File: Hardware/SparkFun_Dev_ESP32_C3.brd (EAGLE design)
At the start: 17.8 x 33 mm, 37 parts, among them J1 USB Female Type C Connector, J4 QWIIC_RIGHT_ANGLE, U1 ESP32-C3, U2 RT9080-33GJ5, Y1 40MHZ

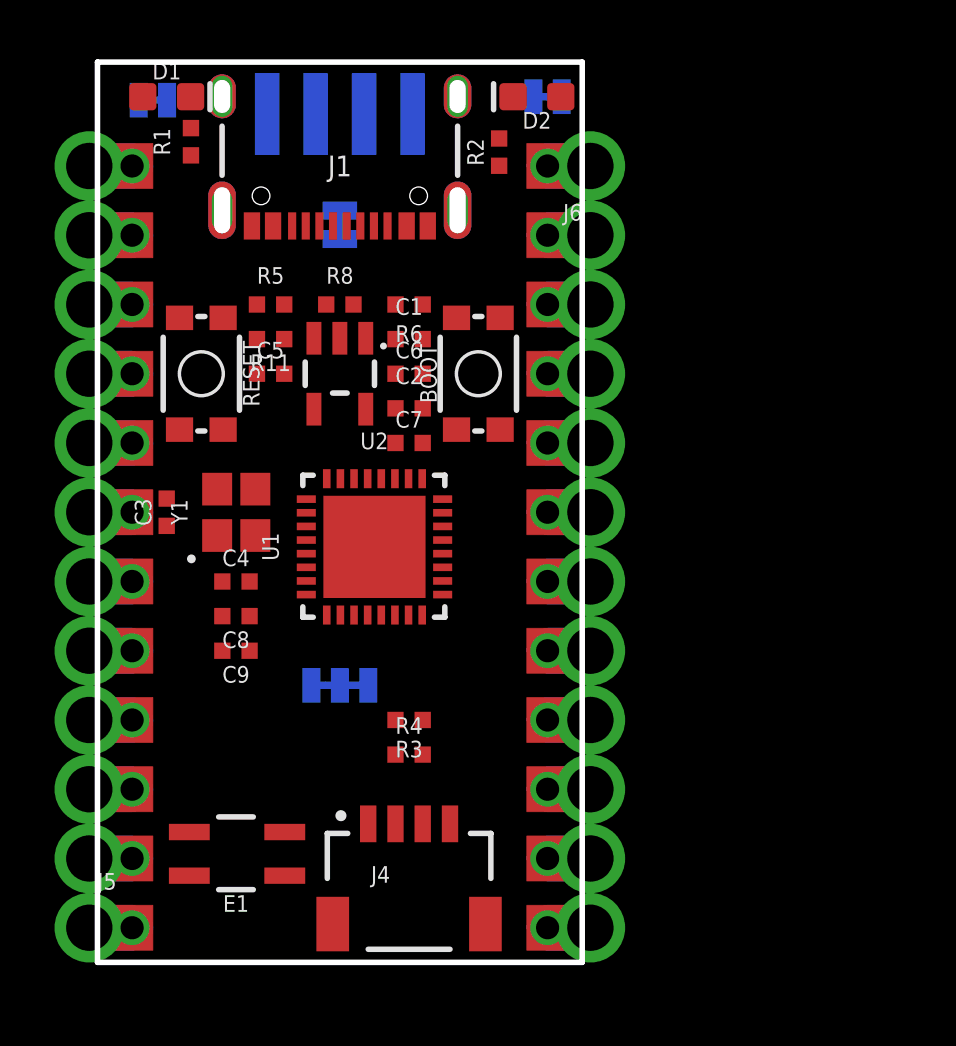
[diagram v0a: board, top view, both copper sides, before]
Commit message: Adds JTAG header and corrects boot control configuration
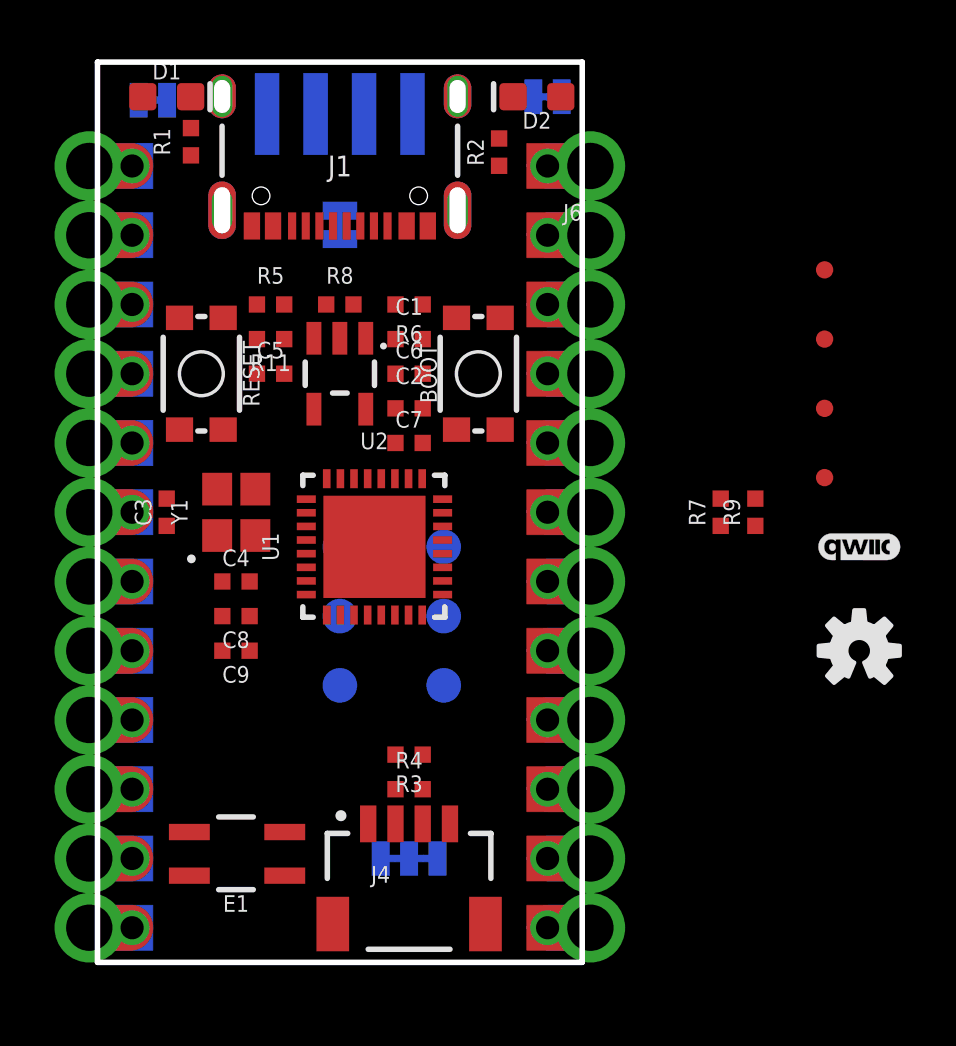
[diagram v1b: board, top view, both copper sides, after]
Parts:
- added FD1, FD2, FD3, FD4: FIDUCIALUFIDUCIAL, SparkFun-Aesthetics:FIDUCIAL-MICRO
- added LOGO2: QWIIC_LOGO_3MM, SparkFun-Aesthetics:QWIIC_3MM
- added LOGO3: OSHW-LOGOS, SparkFun-Aesthetics:OSHW-LOGO-S
- added R7, R9: 100k, SparkFun-Resistors:0402-TIGHT
- added TP1, TP2, TP3, TP4, TP5, TP6: TEST-POINT3X5, SparkFun-Connectors:PAD.03X.05
- moved J5 27.9 mm to (2.54, 29.2), flipped to the bottom, turned to 180 degrees
- moved I2C 6.84 mm to (12.7, 3.81)
- moved R3 1.27 mm to (12.7, 7.62)
- moved R4 1.27 mm to (12.7, 6.35)
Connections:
- removed net IO20/TX: J5.12, J5.12B, U1.P27
- removed net IO21/RX: J5.11, J5.11B, U1.P28
- removed net IO4/A4: U1.P9
- removed net IO5/A5: J6.6, J6.6B, U1.P10
- removed net IO6/SCLK: J6.9, J6.9B, U1.P12
- removed net IO7/PICO: J6.11, J6.11B, U1.P13
- removed net IO8/BOOT: BOOT.3, BOOT.4, C6.1, U1.P14
- new net IO20/TXO: U1.P27
- new net IO21/RXI: U1.P28
- new net IO4/A4/MTMS: J6.5, J6.5B, TP4.1, U1.P9
- new net IO5/A5/MTDI: TP6.1, U1.P10
- new net IO6/SCLK/MTCK: J6.9, J6.9B, TP3.1, U1.P12
- new net IO7/PICO/MTDO: J6.11, J6.11B, TP1.1, U1.P13
- new net IO8: R7.1, U1.P14
- new net IO9/BOOT: BOOT.3, BOOT.4, C6.1, U1.P15
- new net NC: J5.10, J5.10B, J5.9, J5.9B
- net 3.3V: now also R7.2, R9.2
- net EN: now also TP5.1
- net GND: now also J5.3, J5.3B, J5.4, J5.4B, TP2.1; no longer J5.10, J5.10B, J5.9, J5.9B
- net IO10: no longer J5.8, J5.8B
- net IO12: no longer J5.7, J5.7B
- net IO13/SDA: no longer J5.2, J5.2B
- net IO14/SCL: no longer J5.1, J5.1B
- net IO15: no longer J5.6, J5.6B
- net IO16: no longer J5.5, J5.5B
- net IO2/POCI: now also R9.1
- net IO3/A3: now also J6.6, J6.6B; no longer J6.5, J6.5B

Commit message: Moves any connections away from antenna
* Finishes netting
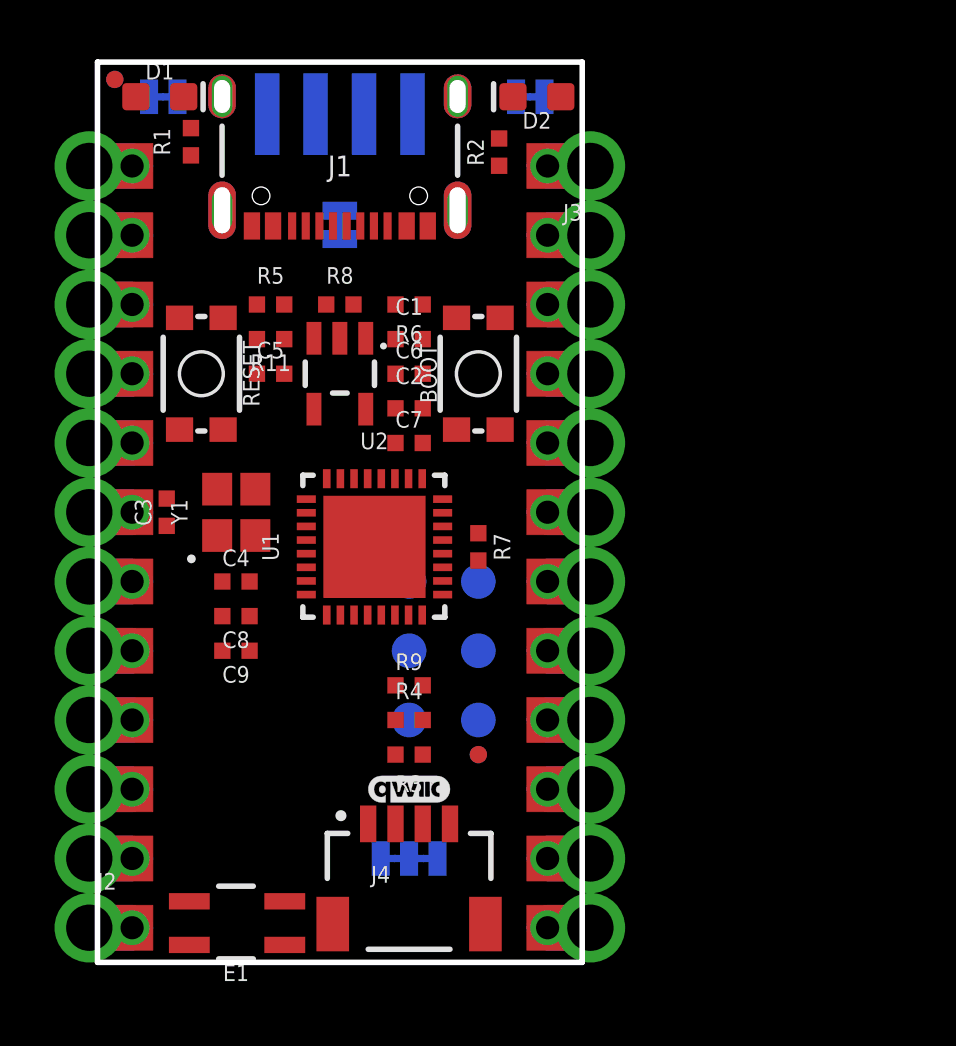
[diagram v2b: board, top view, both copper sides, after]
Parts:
- removed J5, J6: (no value), Castellated:1X12_CASTELLATED
- added J2, J3: (no value), SparkFun-Connectors:1X12_CASTELLATED
- moved FD2 27.7 mm to (1.91, 32.4), flipped to the bottom
- moved FD1 27.0 mm to (1.91, 32.4)
- moved LOGO3 23.0 mm to (6.35, 8.89), flipped to the bottom
- moved LOGO2 18.8 mm to (12.7, 6.35)
- moved FD3 18.0 mm to (15.2, 7.62)
- moved FD4 16.3 mm to (15.2, 7.62), flipped to the bottom
- moved R9 14.2 mm to (12.7, 10.2), turned to 0 degrees
- moved R7 8.98 mm to (15.2, 15.2), turned to 270 degrees
- moved TP4 2.84 mm to (12.7, 8.89)
- moved TP5 2.84 mm to (12.7, 11.4)
- moved TP6 2.84 mm to (12.7, 14.0)
- moved R4 2.54 mm to (12.7, 8.89)
- moved E1 2.54 mm to (6.35, 1.27)
- moved TP1 1.80 mm to (15.2, 14.0)
- moved TP2 1.80 mm to (15.2, 11.4)
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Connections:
- removed net !RESET!: J6.3, J6.3B
- removed net IO6/SDA: J4.3
- removed net IO7/SCL: J4.4
- removed net RAW: J6.1, J6.1B
- net 3.3V: now also J3.4, J3.4B; no longer J6.4, J6.4B
- net EN: now also J3.3, J3.3B
- net GND: now also J2.10, J2.10B, J2.9, J2.9B, J3.2, J3.2B; no longer J5.3, J5.3B, J5.4, J5.4B, J6.2, J6.2B
- net IO0/A0: now also J3.8, J3.8B; no longer J6.8, J6.8B
- net IO1/A1: now also J3.7, J3.7B; no longer J6.7, J6.7B
- net IO10: now also J2.6, J2.6B
- net IO12: now also J2.5, J2.5B
- net IO13/SDA: now also J2.8, J2.8B, J4.3
- net IO14/SCL: now also J2.7, J2.7B, J4.4
- net IO15: now also J2.4, J2.4B
- net IO16: now also J2.3, J2.3B
- net IO2/POCI: now also J3.10, J3.10B; no longer J6.10, J6.10B
- net IO20/TXO: now also J2.12, J2.12B
- net IO21/RXI: now also J2.11, J2.11B
- net IO3/A3: now also J3.6, J3.6B; no longer J6.6, J6.6B
- net IO4/A4/MTMS: now also J3.5, J3.5B; no longer J6.5, J6.5B
- net IO5/A5/MTDI: now also J3.12, J3.12B
- net IO6/SCLK/MTCK: now also J3.9, J3.9B; no longer J6.9, J6.9B
- net IO7/PICO/MTDO: now also J3.11, J3.11B; no longer J6.11, J6.11B
- net NC: now also J2.1, J2.1B, J2.2, J2.2B; no longer J5.10, J5.10B, J5.9, J5.9B
- net V_USB: now also J3.1, J3.1B
